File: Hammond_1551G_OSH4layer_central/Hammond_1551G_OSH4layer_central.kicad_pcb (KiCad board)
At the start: 4 copper layers, 44 x 29 mm, 4 parts

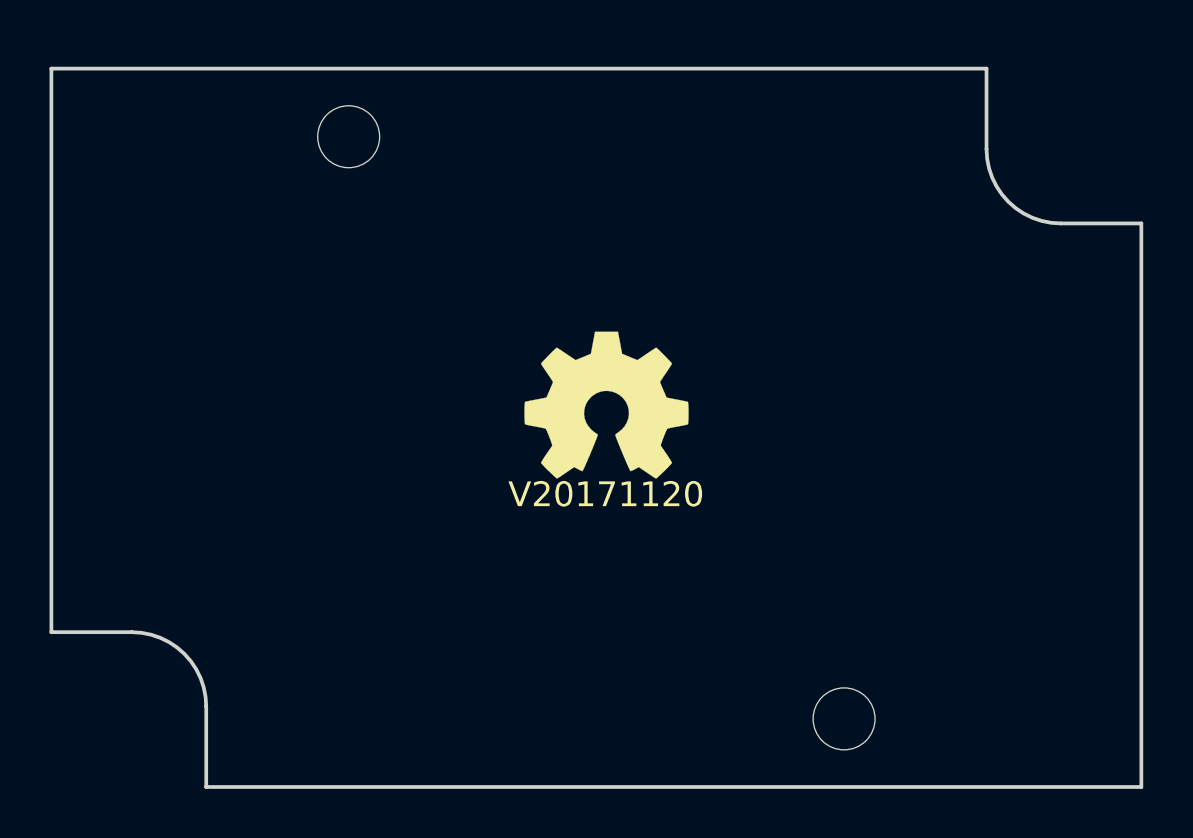
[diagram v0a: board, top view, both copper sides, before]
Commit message: DONE: Hammond 1551G, 4 layer, connectored microcontroller template
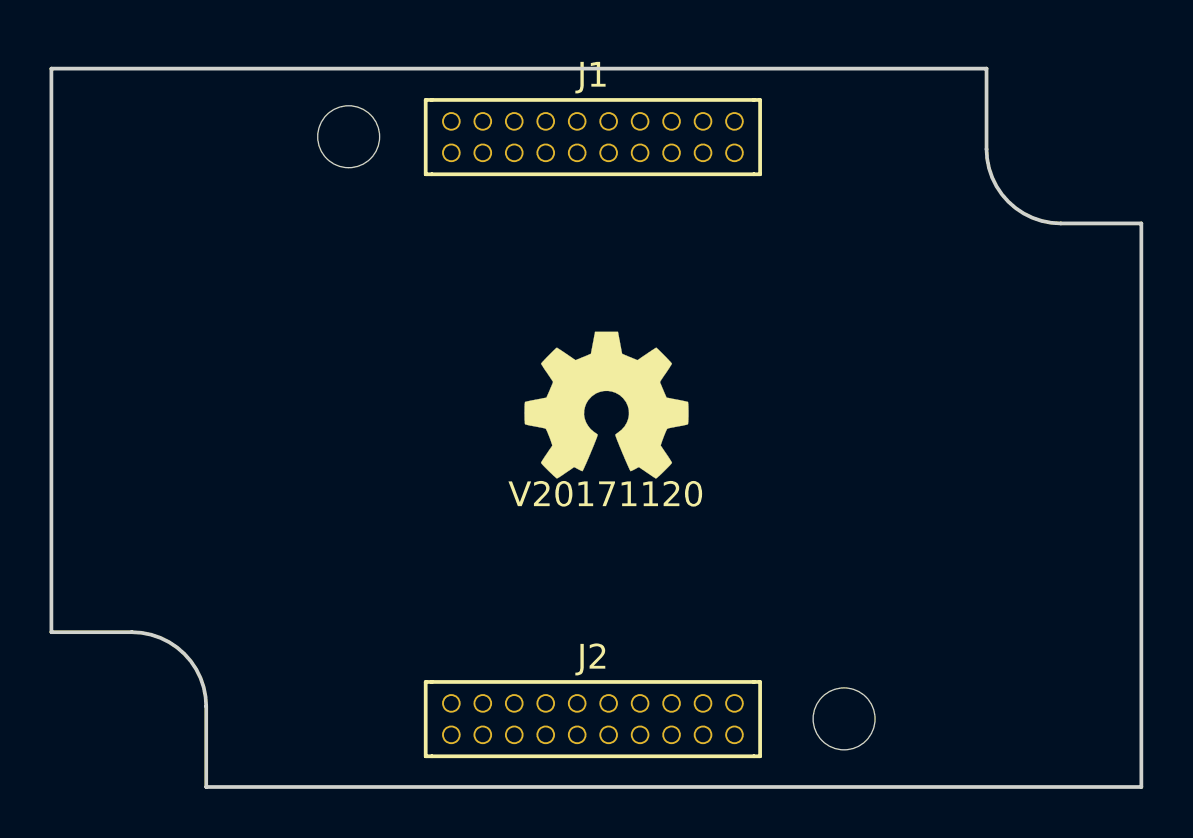
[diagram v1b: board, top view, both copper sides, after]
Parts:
- added J1: Conn_02x10_Odd_Even, SquantorConnectors:Header_0127_2X10_H007, F.Cu at (149.9, 88.3)
- added J2: Conn_02x10_Odd_Even, SquantorConnectors:Header_0127_2X10_H007, F.Cu at (149.9, 111.8)
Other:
- rule pad_to_mask_clearance: 0.2 -> 0.1

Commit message: DONE: updated header footprints
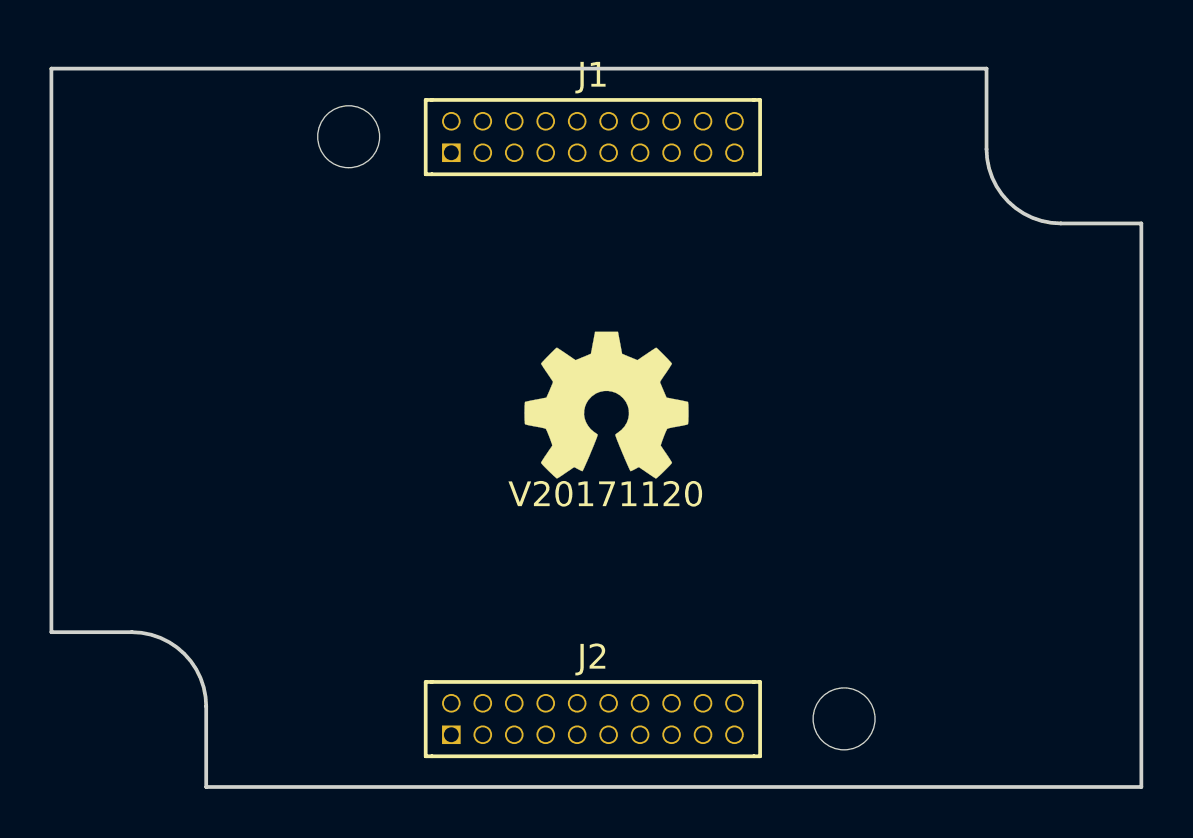
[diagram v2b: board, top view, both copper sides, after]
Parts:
- J1, J2: footprint SquantorConnectors:Header_0127_2X10_H007 -> SquantorConnectors:Header-0127-2X10-H006
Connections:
- net Net-(J1-Pad10) renamed /ANALOG_05
- net Net-(J1-Pad11) renamed /ANALOG_06
- net Net-(J1-Pad12) renamed /ANALOG_07
- net Net-(J1-Pad13) renamed /ANALOG_08
- net Net-(J1-Pad14) renamed /ANALOG_09
- net Net-(J1-Pad15) renamed /ANALOG_10
- net Net-(J1-Pad16) renamed /ANALOG_11
- net Net-(J1-Pad17) renamed /ANALOG_12
- net Net-(J1-Pad18) renamed /ANALOG_13
- net Net-(J1-Pad19) renamed /ANALOG_14
- net Net-(J1-Pad20) renamed /ANALOG_15
- net Net-(J1-Pad5) renamed /ANALOG_00
- net Net-(J1-Pad6) renamed /ANALOG_01
- net Net-(J1-Pad7) renamed /ANALOG_02
- net Net-(J1-Pad8) renamed /ANALOG_03
- net Net-(J1-Pad9) renamed /ANALOG_04
- net Net-(J2-Pad10) renamed /DIGITAL_05
- net Net-(J2-Pad11) renamed /DIGITAL_06
- net Net-(J2-Pad12) renamed /DIGITAL_07
- net Net-(J2-Pad13) renamed /DIGITAL_08
- net Net-(J2-Pad14) renamed /DIGITAL_09
- net Net-(J2-Pad15) renamed /DIGITAL_10
- net Net-(J2-Pad16) renamed /DIGITAL_11
- net Net-(J2-Pad17) renamed /DIGITAL_12
- net Net-(J2-Pad18) renamed /DIGITAL_13
- net Net-(J2-Pad19) renamed /DIGITAL_14
- net Net-(J2-Pad20) renamed /DIGITAL_15
- net Net-(J2-Pad5) renamed /DIGITAL_00
- net Net-(J2-Pad6) renamed /DIGITAL_01
- net Net-(J2-Pad7) renamed /DIGITAL_02
- net Net-(J2-Pad8) renamed /DIGITAL_03
- net Net-(J2-Pad9) renamed /DIGITAL_04
